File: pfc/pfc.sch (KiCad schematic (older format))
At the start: 36 parts, among them J1 Conn_01x03_Male, J2 CONN_01X02, U1 NFET, U2 NFET, U3 BD7692FJ

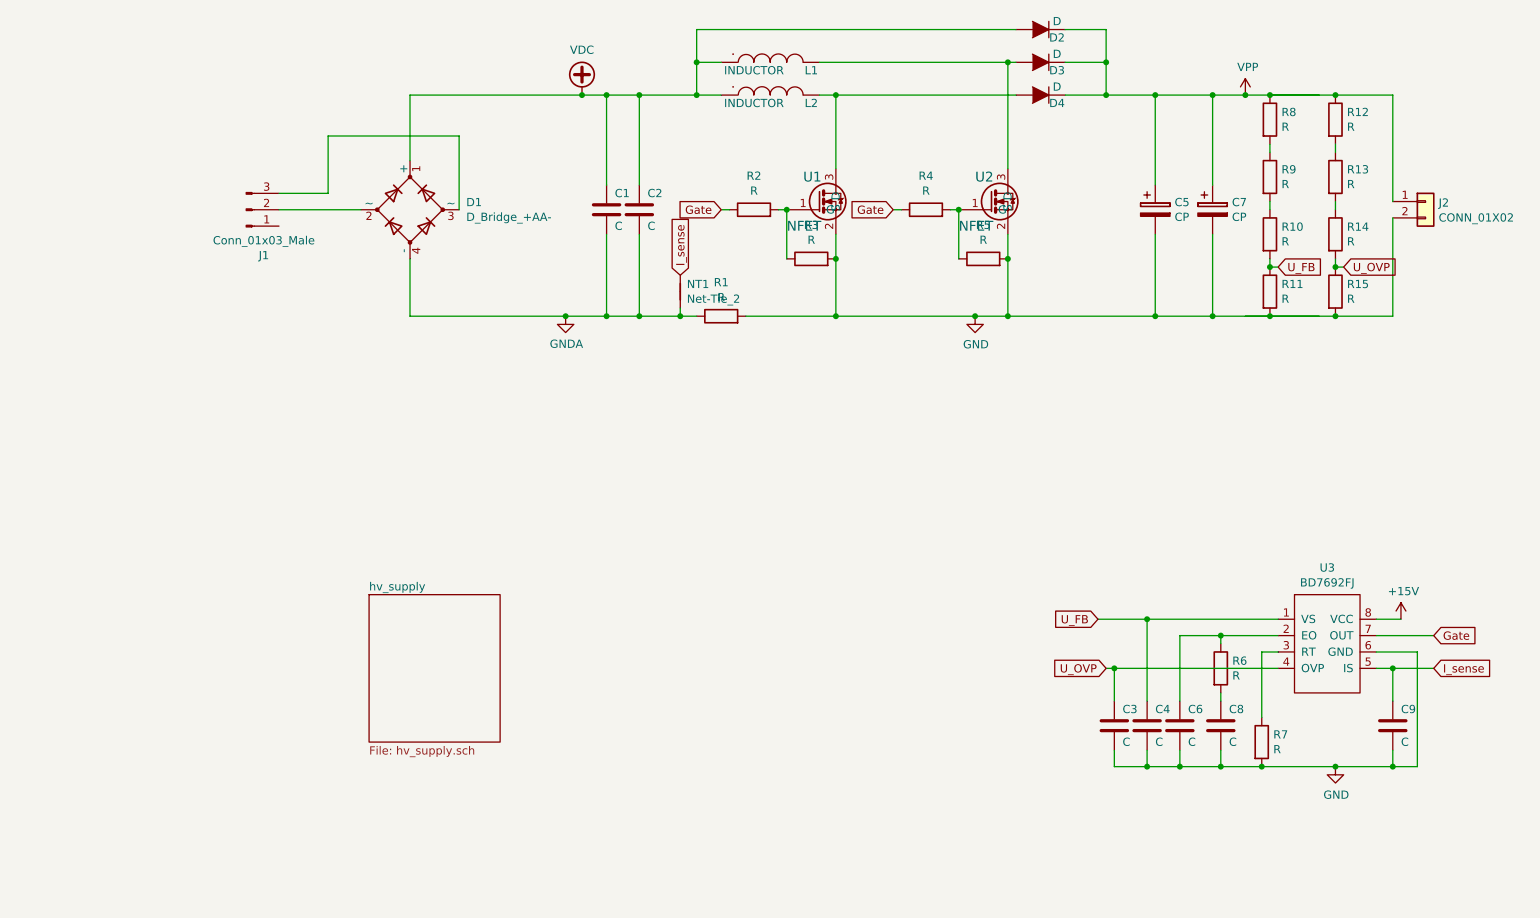
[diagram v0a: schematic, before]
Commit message: add component values and mounting hole
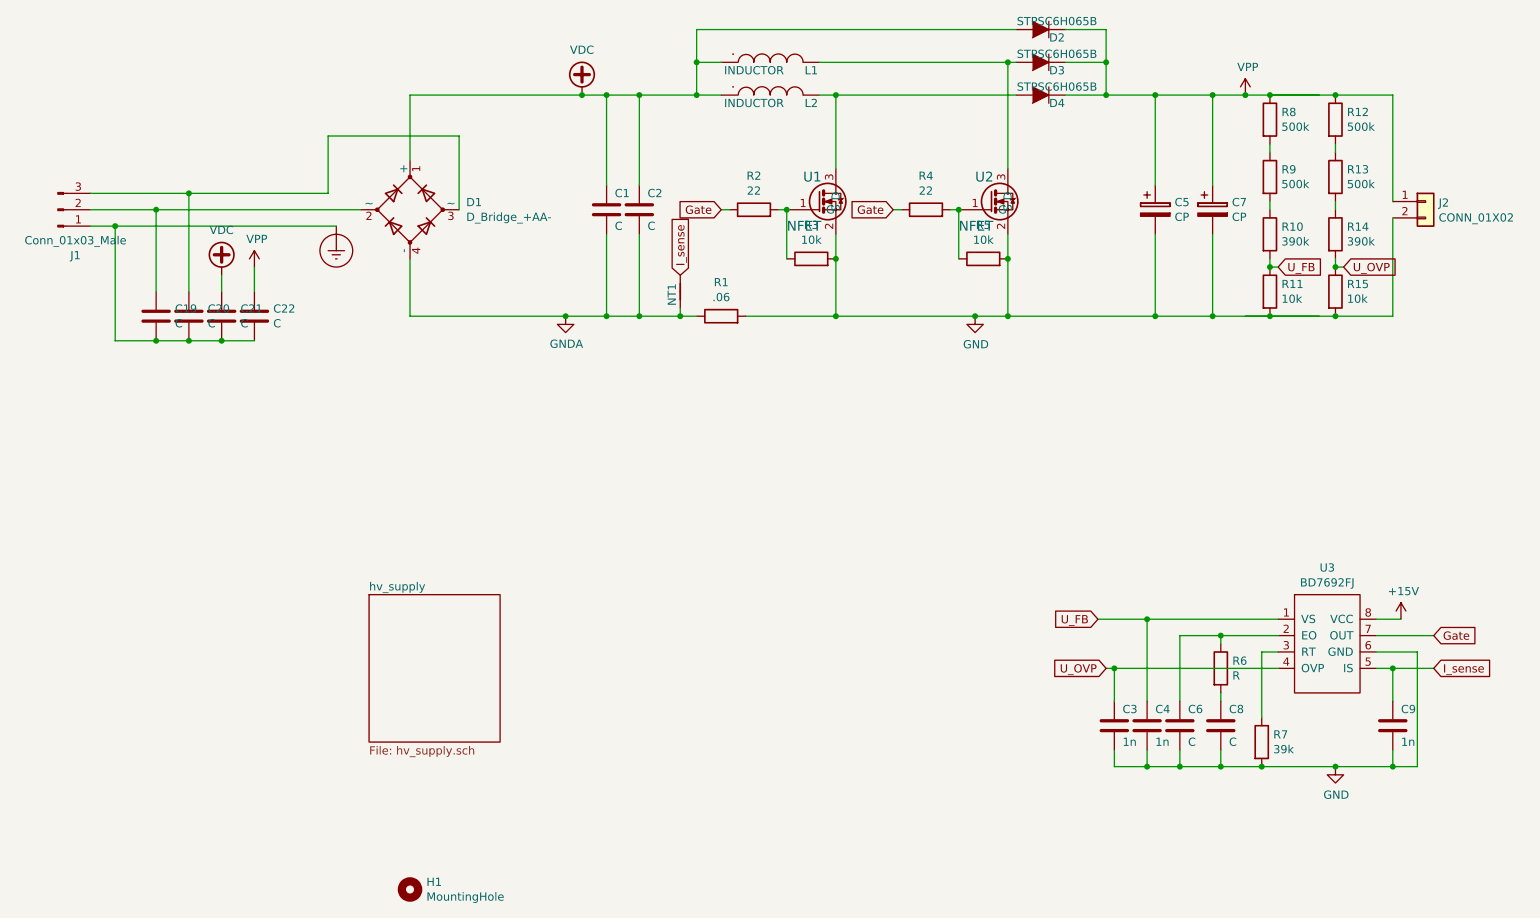
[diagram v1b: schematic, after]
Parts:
- added C19, C20, C21, C22: C, stmbl-kicad-lib:C_1808, symbol Device:C
- added H1: MountingHole, MountingHole:MountingHole_3mm, symbol Mechanical:MountingHole
- C3, C4, C9: value C -> 1n
- D2, D3, D4: value D -> STPSC6H065B
- R1: value R -> .06
- R10, R14: value R -> 390k
- R11, R15, R3, R5: value R -> 10k
- R12, R13, R8, R9: value R -> 500k
- R2, R4: value R -> 22
- R7: value R -> 39k
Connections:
- net labels added: Earth_Protective
- wire segments 110 -> 123
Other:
- moved on the sheet: J1
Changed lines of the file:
@@
 Connection ~ 3950 2500
 Connection ~ 4050 1150
-Wire Wire Line
-	2200 1750 2500 1750
-Wire Wire Line
-	2200 1850 2700 1850
+Connection ~ 1450 1850
+Connection ~ 1650 1750
+Connection ~ 1200 1950
+Connection ~ 1450 2650
+Connection ~ 1650 2650
+Connection ~ 1850 2650
+Wire Wire Line
+	1050 1750 1650 1750
+Wire Wire Line
+	1050 1850 1450 1850
+Wire Wire Line
+	1050 1950 1200 1950
+Wire Wire Line
+	1200 1950 1200 2650
+Wire Wire Line
+	1200 1950 2550 1950
+Wire Wire Line
+	1200 2650 1450 2650
+Wire Wire Line
+	1450 1850 1450 2350
+Wire Wire Line
+	1450 1850 2700 1850
+Wire Wire Line
+	1450 2650 1650 2650
+Wire Wire Line
+	1650 1750 1650 2350
+Wire Wire Line
+	1650 1750 2500 1750
+Wire Wire Line
+	1650 2650 1850 2650
+Wire Wire Line
+	1850 2250 1850 2350
+Wire Wire Line
+	1850 2650 2050 2650
+Wire Wire Line
+	2050 2200 2050 2350
 Wire Wire Line
 	2500 1400 3300 1400
@@
 U 1 1 5EA4A187
 P 4650 2350
-F 0 "NT1" V 4695 2310 50  0000 R CNN
-F 1 "Net-Tie_2" V 4605 2310 50  0000 R CNN
+F 0 "NT1" H 4700 2400 50  0000 R CNN
+F 1 "Net-Tie_2" V 4250 2550 50  0001 R CNN
 F 2 "NetTie:NetTie-2_SMD_Pad0.5mm" H 4650 2350 50  0001 C CNN
 F 3 "~" H 4650 2350 50  0001 C CNN
 	1    4650 2350
 	0    -1   -1   0
+$EndComp
+$Comp
+L stmbl:VPP #PWR0109
+U 1 1 5EA03BB7
+P 2050 2200
+F 0 "#PWR0109" H 2050 2050 50  0001 C CNN
+F 1 "VPP" H 2065 2370 50  0000 C CNN
+F 2 "" H 2050 2200 50  0001 C CNN
+F 3 "" H 2050 2200 50  0001 C CNN
+	1    2050 2200
+	1    0    0    -1
 $EndComp
 $Comp
@@
 $EndComp
 $Comp
+L Mechanical:MountingHole H1
+U 1 1 5E9F5E62
+P 3000 6000
+F 0 "H1" H 3100 6045 50  0000 L CNN
+F 1 "MountingHole" H 3100 5955 50  0000 L CNN
+F 2 "MountingHole:MountingHole_3mm" H 3000 6000 50  0001 C CNN
+F 3 "~" H 3000 6000 50  0001 C CNN
+	1    3000 6000
+	1    0    0    -1
+$EndComp
+$Comp
 L stmbl:R R1
 U 1 1 5E96EDAC
 P 4900 2500
 F 0 "R1" V 5106 2500 50  0000 C CNN
-F 1 "R" V 5015 2500 50  0000 C CNN
+F 1 ".06" V 5015 2500 50  0000 C CNN
 F 2 "stmbl-kicad-lib:R_2512_BIG" V 4830 2500 50  0001 C CNN
 F 3 "" H 4900 2500 50  0000 C CNN
@@
 P 5100 1850
 F 0 "R2" V 5306 1850 50  0000 C CNN
-F 1 "R" V 5215 1850 50  0000 C CNN
+F 1 "22" V 5215 1850 50  0000 C CNN
 F 2 "stmbl-kicad-lib:R_0805" V 5030 1850 50  0001 C CNN
 F 3 "" H 5100 1850 50  0000 C CNN
@@
 P 5450 2150
 F 0 "R3" V 5656 2150 50  0000 C CNN
-F 1 "R" V 5565 2150 50  0000 C CNN
+F 1 "10k" V 5565 2150 50  0000 C CNN
 F 2 "stmbl-kicad-lib:R_0805" V 5380 2150 50  0001 C CNN
 F 3 "" H 5450 2150 50  0000 C CNN
@@
 P 6150 1850
 F 0 "R4" V 6356 1850 50  0000 C CNN
-F 1 "R" V 6265 1850 50  0000 C CNN
+F 1 "22" V 6265 1850 50  0000 C CNN
 F 2 "stmbl-kicad-lib:R_0805" V 6080 1850 50  0001 C CNN
 F 3 "" H 6150 1850 50  0000 C CNN
@@
 P 6500 2150
 F 0 "R5" V 6706 2150 50  0000 C CNN
-F 1 "R" V 6615 2150 50  0000 C CNN
+F 1 "10k" V 6615 2150 50  0000 C CNN
 F 2 "stmbl-kicad-lib:R_0805" V 6430 2150 50  0001 C CNN
 F 3 "" H 6500 2150 50  0000 C CNN
@@
 P 8200 5100
 F 0 "R7" H 8270 5145 50  0000 L CNN
-F 1 "R" H 8270 5055 50  0000 L CNN
+F 1 "39k" H 8270 5055 50  0000 L CNN
 F 2 "stmbl-kicad-lib:C_0603" V 8130 5100 50  0001 C CNN
 F 3 "" H 8200 5100 50  0001 C CNN
@@
 P 8250 1300
 F 0 "R8" H 8320 1345 50  0000 L CNN
-F 1 "R" H 8320 1255 50  0000 L CNN
+F 1 "500k" H 8320 1255 50  0000 L CNN
 F 2 "stmbl-kicad-lib:R_0805" V 8180 1300 50  0001 C CNN
 F 3 "" H 8250 1300 50  0000 C CNN
@@
 P 8250 1650
 F 0 "R9" H 8320 1695 50  0000 L CNN
-F 1 "R" H 8320 1605 50  0000 L CNN
+F 1 "500k" H 8320 1605 50  0000 L CNN
 F 2 "stmbl-kicad-lib:R_0805" V 8180 1650 50  0001 C CNN
 F 3 "" H 8250 1650 50  0000 C CNN
@@
 P 8250 2000
 F 0 "R10" H 8320 2045 50  0000 L CNN
-F 1 "R" H 8320 1955 50  0000 L CNN
+F 1 "390k" H 8320 1955 50  0000 L CNN
 F 2 "stmbl-kicad-lib:R_0805" V 8180 2000 50  0001 C CNN
 F 3 "" H 8250 2000 50  0000 C CNN
@@
 P 8250 2350
 F 0 "R11" H 8320 2395 50  0000 L CNN
-F 1 "R" H 8320 2305 50  0000 L CNN
+F 1 "10k" H 8320 2305 50  0000 L CNN
 F 2 "stmbl-kicad-lib:R_0805" V 8180 2350 50  0001 C CNN
 F 3 "" H 8250 2350 50  0000 C CNN
@@
 P 8650 1300
 F 0 "R12" H 8720 1345 50  0000 L CNN
-F 1 "R" H 8720 1255 50  0000 L CNN
+F 1 "500k" H 8720 1255 50  0000 L CNN
 F 2 "stmbl-kicad-lib:R_0805" V 8580 1300 50  0001 C CNN
 F 3 "" H 8650 1300 50  0000 C CNN
@@
 P 8650 1650
 F 0 "R13" H 8720 1695 50  0000 L CNN
-F 1 "R" H 8720 1605 50  0000 L CNN
+F 1 "500k" H 8720 1605 50  0000 L CNN
 F 2 "stmbl-kicad-lib:R_0805" V 8580 1650 50  0001 C CNN
 F 3 "" H 8650 1650 50  0000 C CNN
@@
 P 8650 2000
 F 0 "R14" H 8720 2045 50  0000 L CNN
-F 1 "R" H 8720 1955 50  0000 L CNN
+F 1 "390k" H 8720 1955 50  0000 L CNN
 F 2 "stmbl-kicad-lib:R_0805" V 8580 2000 50  0001 C CNN
 F 3 "" H 8650 2000 50  0000 C CNN
@@
 P 8650 2350
 F 0 "R15" H 8720 2395 50  0000 L CNN
-F 1 "R" H 8720 2305 50  0000 L CNN
+F 1 "10k" H 8720 2305 50  0000 L CNN
 F 2 "stmbl-kicad-lib:R_0805" V 8580 2350 50  0001 C CNN
 F 3 "" H 8650 2350 50  0000 C CNN
@@
 P 6850 750
 F 0 "D2" H 6750 800 50  0000 C CNN
-F 1 "D" H 6750 700 50  0000 C CNN
+F 1 "STPSC6H065B" H 6750 700 50  0000 C CNN
 F 2 "stmbl-kicad-lib:TO-252-2_STSiC" H 6850 750 50  0001 C CNN
 F 3 "" H 6850 750 50  0000 C CNN
@@
 P 6850 950
 F 0 "D3" H 6750 1000 50  0000 C CNN
-F 1 "D" H 6750 900 50  0000 C CNN
+F 1 "STPSC6H065B" H 6750 900 50  0000 C CNN
 F 2 "stmbl-kicad-lib:TO-252-2_STSiC" H 6850 950 50  0001 C CNN
 F 3 "" H 6850 950 50  0000 C CNN
@@
 P 6850 1150
 F 0 "D4" H 6750 1200 50  0000 C CNN
-F 1 "D" H 6750 1100 50  0000 C CNN
+F 1 "STPSC6H065B" H 6750 1100 50  0000 C CNN
 F 2 "stmbl-kicad-lib:TO-252-2_STSiC" H 6850 1150 50  0001 C CNN
 F 3 "" H 6850 1150 50  0000 C CNN
 	1    6850 1150
 	-1   0    0    1
+$EndComp
+$Comp
+L stmbl:VDC #PWR0107
+U 1 1 5EA00B8A
+P 1850 2250
+F 0 "#PWR0107" H 1850 2150 50  0001 C CNN
+F 1 "VDC" H 1850 2525 50  0000 C CNN
+F 2 "" H 1850 2250 50  0001 C CNN
+F 3 "" H 1850 2250 50  0001 C CNN
+	1    1850 2250
+	1    0    0    -1
 $EndComp
 $Comp
@@
 $EndComp
 $Comp
+L stmbl:Earth_Protective #PWR0108
+U 1 1 5E9FAE60
+P 2550 1950
+F 0 "#PWR0108" H 2800 1700 50  0001 C CNN
+F 1 "Earth_Protective" H 3000 1800 50  0001 C CNN
+F 2 "" H 2550 1850 50  0001 C CNN
+F 3 "" H 2550 1850 50  0001 C CNN
+	1    2550 1950
+	1    0    0    -1
+$EndComp
+$Comp
 L stmbl:CONN_01X02 J2
 U 1 1 5E97E98C
@@
 $EndComp
 $Comp
+L Device:C C19
+U 1 1 5E9FF932
+P 1450 2500
+F 0 "C19" H 1565 2545 50  0000 L CNN
+F 1 "C" H 1565 2455 50  0000 L CNN
+F 2 "stmbl-kicad-lib:C_1808" H 1488 2350 50  0001 C CNN
+F 3 "~" H 1450 2500 50  0001 C CNN
+	1    1450 2500
+	1    0    0    -1
+$EndComp
+$Comp
+L Device:C C20
+U 1 1 5E9FEE4F
+P 1650 2500
+F 0 "C20" H 1765 2545 50  0000 L CNN
+F 1 "C" H 1765 2455 50  0000 L CNN
+F 2 "stmbl-kicad-lib:C_1808" H 1688 2350 50  0001 C CNN
+F 3 "~" H 1650 2500 50  0001 C CNN
+	1    1650 2500
+	1    0    0    -1
+$EndComp
+$Comp
+L Device:C C21
+U 1 1 5E9FE3EE
+P 1850 2500
+F 0 "C21" H 1965 2545 50  0000 L CNN
+F 1 "C" H 1965 2455 50  0000 L CNN
+F 2 "stmbl-kicad-lib:C_1808" H 1888 2350 50  0001 C CNN
+F 3 "~" H 1850 2500 50  0001 C CNN
+	1    1850 2500
+	1    0    0    -1
+$EndComp
+$Comp
+L Device:C C22
+U 1 1 5E9FDA2F
+P 2050 2500
+F 0 "C22" H 2165 2545 50  0000 L CNN
+F 1 "C" H 2165 2455 50  0000 L CNN
+F 2 "stmbl-kicad-lib:C_1808" H 2088 2350 50  0001 C CNN
+F 3 "~" H 2050 2500 50  0001 C CNN
+	1    2050 2500
+	1    0    0    -1
+$EndComp
+$Comp
 L stmbl:C C1
 U 1 1 5E97AD62
@@
 P 7300 5000
 F 0 "C3" H 7350 5100 50  0000 L CNN
-F 1 "C" H 7350 4900 50  0000 L CNN
+F 1 "1n" H 7350 4900 50  0000 L CNN
 F 2 "stmbl-kicad-lib:C_0603" H 7338 4850 50  0001 C CNN
 F 3 "" H 7300 5000 50  0001 C CNN
@@
 P 7500 5000
 F 0 "C4" H 7550 5100 50  0000 L CNN
-F 1 "C" H 7550 4900 50  0000 L CNN
+F 1 "1n" H 7550 4900 50  0000 L CNN
 F 2 "stmbl-kicad-lib:C_0603" H 7538 4850 50  0001 C CNN
 F 3 "" H 7500 5000 50  0001 C CNN
@@
 P 9000 5000
 F 0 "C9" H 9050 5100 50  0000 L CNN
-F 1 "C" H 9050 4900 50  0000 L CNN
+F 1 "1n" H 9050 4900 50  0000 L CNN
 F 2 "stmbl-kicad-lib:C_0603" H 9038 4850 50  0001 C CNN
 F 3 "" H 9000 5000 50  0001 C CNN
@@
 L Connector:Conn_01x03_Male J1
 U 1 1 5E98A2AD
-P 2000 1850
-F 0 "J1" H 2108 2129 50  0000 C CNN
-F 1 "Conn_01x03_Male" H 2108 2038 50  0000 C CNN
-F 2 "stmbl-kicad-lib:RM7.62_1x3" H 2000 1850 50  0001 C CNN
-F 3 "~" H 2000 1850 50  0001 C CNN
-	1    2000 1850
+P 850 1850
+F 0 "J1" H 958 2129 50  0000 C CNN
+F 1 "Conn_01x03_Male" H 958 2038 50  0000 C CNN
+F 2 "stmbl-kicad-lib:RM7.62_1x3" H 850 1850 50  0001 C CNN
+F 3 "~" H 850 1850 50  0001 C CNN
+	1    850  1850
 	1    0    0    1
 $EndComp
